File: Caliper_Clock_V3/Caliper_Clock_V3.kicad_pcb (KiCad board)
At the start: 2 copper layers, 55 x 25 mm, 22 parts, among them J1 LCD PADS, J2 SBW, SW1 MODE, SW2 HOUR, SW3 MIN, U1 TPS61099DRVR, U2 MSP430FR4133IPM, Y1 32.768kHz

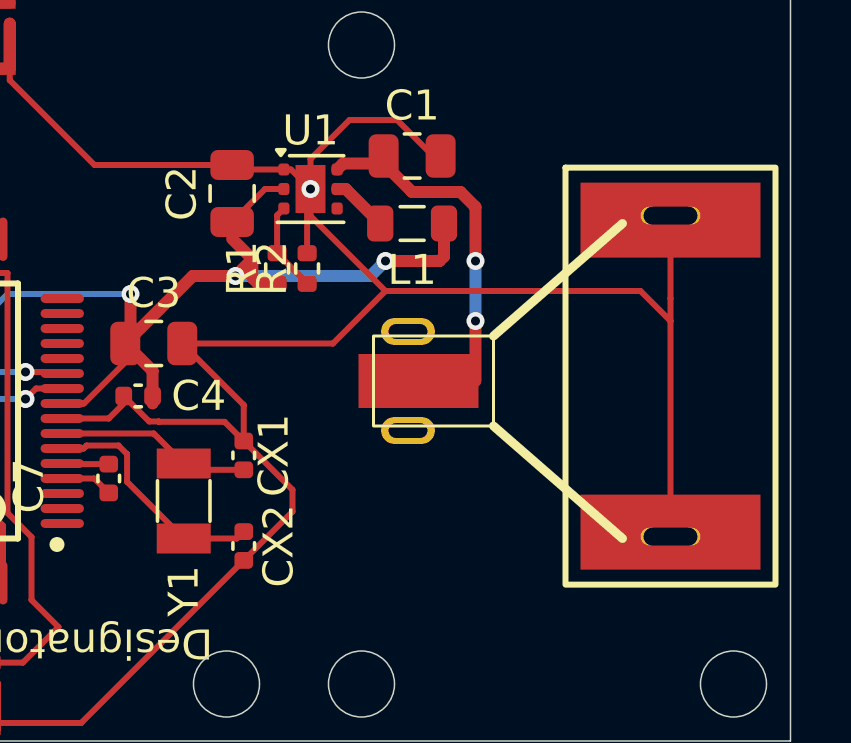
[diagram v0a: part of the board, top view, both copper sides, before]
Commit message: hw: fix boost inductor rail; re-route and regen fab outputs
Fix the inductor (L1) wiring on the TPS61099 boost: it was tied to
+3V0 (VOUT) instead of +BATT (VIN), so there was no inductor path from
the cell into SW and the +3V0 rail stayed dead. Schematic now ties L1 to
+BATT. This was the root cause of the dead / 0.1 V rail (bench-confirmed
by jumpering L1 to +BATT, which brought +3V0 up to 3.0 V).

Re-route the PCB for the corrected net and regenerate Gerbers2/ + BOM/CPL
for the next fab spin.
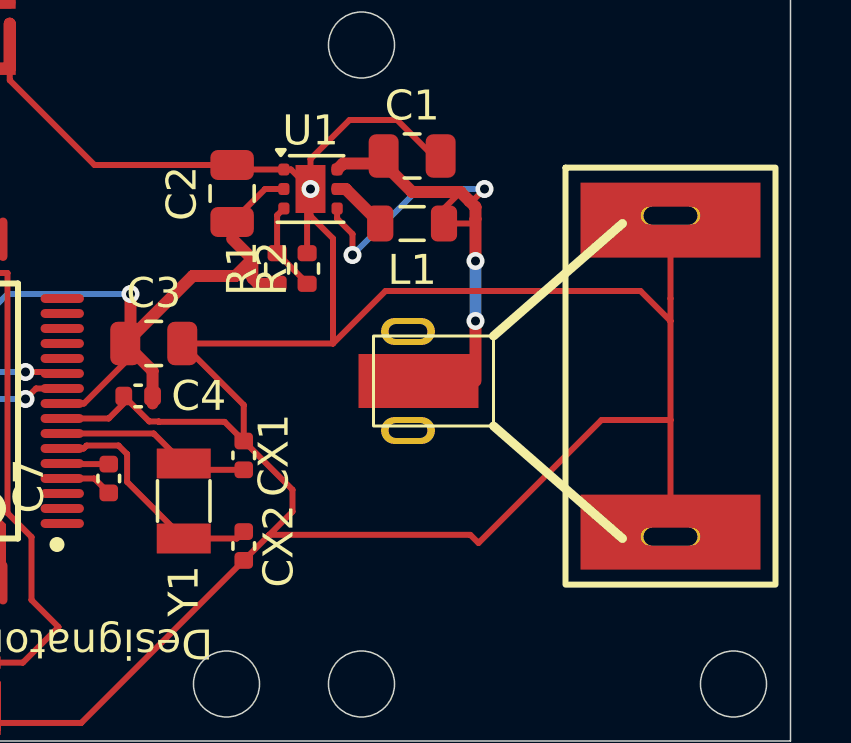
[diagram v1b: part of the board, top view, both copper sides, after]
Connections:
- L1 pad 1: +3V0 -> +BATT
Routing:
- net GND: track 116.5 -> 132.8 mm
- net +BATT: track 11.8 -> 21.9 mm, vias 2 -> 4
- net +3V0: track 66.4 -> 58.0 mm, vias 6 -> 4
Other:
- board text added: "BLAKE HORD 2026 CALIPER CLOCK V3.2"
- board text removed: "BLAKE HORD 2026 CALIPER CLOCK V3.0"
